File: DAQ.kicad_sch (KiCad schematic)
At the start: 32 parts, among them IC2 TEENSY_4.1, SW1 SW_Push_Open, SW2 SW_Push_Open, U3 CD-PA1616D

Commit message: added display
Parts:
- added U4: ~, symbol DAQcustom:NX4024T032
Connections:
- net +5V: now also U4.1 (Vdd)
- net GND: now also U4.2 (GND)
- net at IC2.28 (RX7): now also U4.4 (TX)
- net at IC2.29 (TX7): now also U4.3 (RX)
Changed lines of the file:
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@@
+    (stroke (width 0) (type default))
+  )
+  (wire (pts (xy 143.51 129.54) (xy 152.4 129.54))
     (stroke (width 0) (type default))
   )
@@
     (stroke (width 0) (type default))
   )
+  (wire (pts (xy 110.49 167.64) (xy 116.84 167.64))
+    (stroke (width 0) (type default))
+  )
   (wire (pts (xy 67.31 93.98) (xy 68.58 93.98))
     (stroke (width 0) (type default))
@@
     (stroke (width 0) (type default))
   )
+  (wire (pts (xy 146.05 132.08) (xy 152.4 132.08))
+    (stroke (width 0) (type default))
+  )
   (wire (pts (xy 69.85 148.59) (xy 80.01 148.59))
     (stroke (width 0) (type default))
@@
     (stroke (width 0) (type default))
   )
+  (wire (pts (xy 143.51 163.83) (xy 143.51 129.54))
+    (stroke (width 0) (type default))
+  )
   (polyline (pts (xy 227.33 64.77) (xy 238.76 64.77))
     (stroke (width 0) (type default))
@@
     (stroke (width 0) (type default))
   )
+  (wire (pts (xy 146.05 167.64) (xy 146.05 132.08))
+    (stroke (width 0) (type default))
+  )
   (polyline (pts (xy 118.11 129.54) (xy 118.11 152.4))
     (stroke (width 0) (type default))
@@
     (stroke (width 0) (type default))
   )
+  (wire (pts (xy 132.08 167.64) (xy 146.05 167.64))
+    (stroke (width 0) (type default))
+  )
   (wire (pts (xy 172.72 156.21) (xy 184.15 156.21))
     (stroke (width 0) (type default))
@@
     (stroke (width 0) (type default))
   )
+  (wire (pts (xy 132.08 163.83) (xy 143.51 163.83))
+    (stroke (width 0) (type default))
+  )
   (wire (pts (xy 109.22 78.74) (xy 125.73 78.74))
     (stroke (width 0) (type default))
@@
   )
   (wire (pts (xy 232.41 82.55) (xy 232.41 83.82))
+    (stroke (width 0) (type default))
+  )
+  (wire (pts (xy 110.49 163.83) (xy 116.84 163.83))
     (stroke (width 0) (type default))
   )
@@
     )
   )
+  (symbol (lib_id "power:+5V") (at 110.49 163.83 0) (unit 1)
+    (in_bom yes) (on_board yes) (dnp no) (fields_autoplaced)
+    (property "Reference" "#PWR022" (at 110.49 167.64 0)
+      (effects (font (size 1.27 1.27)) hide)
+    )
+    (property "Value" "+5V" (at 110.49 158.75 0)
+      (effects (font (size 1.27 1.27)))
+    )
+    (property "Footprint" "" (at 110.49 163.83 0)
+      (effects (font (size 1.27 1.27)) hide)
+    )
+    (property "Datasheet" "" (at 110.49 163.83 0)
+      (effects (font (size 1.27 1.27)) hide)
+    )
+    (pin "1")
+    (instances
+      (project "DAQ"
+        (path "/813e588e-265c-47f4-92de-e30a6c3791f8"
+          (reference "#PWR022") (unit 1)
+        )
+      )
+    )
+  )
   (symbol (lib_id "Device:R_Potentiometer") (at 33.02 139.7 0) (unit 1)
     (in_bom yes) (on_board yes) (dnp no) (fields_autoplaced)
@@
         (path "/813e588e-265c-47f4-92de-e30a6c3791f8"
           (reference "#PWR05") (unit 1)
+        )
+      )
+    )
+  )
+  (symbol (lib_id "DAQcustom:NX4024T032") (at 124.46 166.37 0) (unit 1)
+    (in_bom yes) (on_board yes) (dnp no) (fields_autoplaced)
+    (property "Reference" "U4" (at 124.46 157.48 0)
+      (effects (font (size 1.27 1.27)))
+    )
+    (property "Value" "~" (at 124.46 166.37 0)
+      (effects (font (size 1.27 1.27)))
+    )
+    (property "Footprint" "" (at 124.46 166.37 0)
+      (effects (font (size 1.27 1.27)) hide)
+    )
+    (property "Datasheet" "" (at 124.46 166.37 0)
+      (effects (font (size 1.27 1.27)) hide)
+    )
+    (pin "1")
+    (pin "2")
+    (pin "3")
+    (pin "4")
+    (instances
+      (project "DAQ"
+        (path "/813e588e-265c-47f4-92de-e30a6c3791f8"
+          (reference "U4") (unit 1)
         )
       )
@@
         )
       )
+    )
+  )
+  (symbol (lib_id "power:GND") (at 110.49 167.64 0) (unit 1)
+    (in_bom yes) (on_board yes) (dnp no) (fields_autoplaced)
+    (property "Reference" "#PWR023" (at 110.49 173.99 0)
+      (effects (font (size 1.27 1.27)) hide)
+    )
+    (property "Value" "GND" (at 110.49 172.72 0)
+      (effects (font (size 1.27 1.27)))
+    )
+    (property "Footprint" "" (at 110.49 167.64 0)
+      (effects (font (size 1.27 1.27)) hide)
+    )
+    (property "Datasheet" "" (at 110.49 167.64 0)
+      (effects (font (size 1.27 1.27)) hide)
+    )
+    (pin "1")
+    (instances
+      (project "DAQ"
+        (path "/813e588e-265c-47f4-92de-e30a6c3791f8"
+          (reference "#PWR023") (unit 1)
+        )
+      )

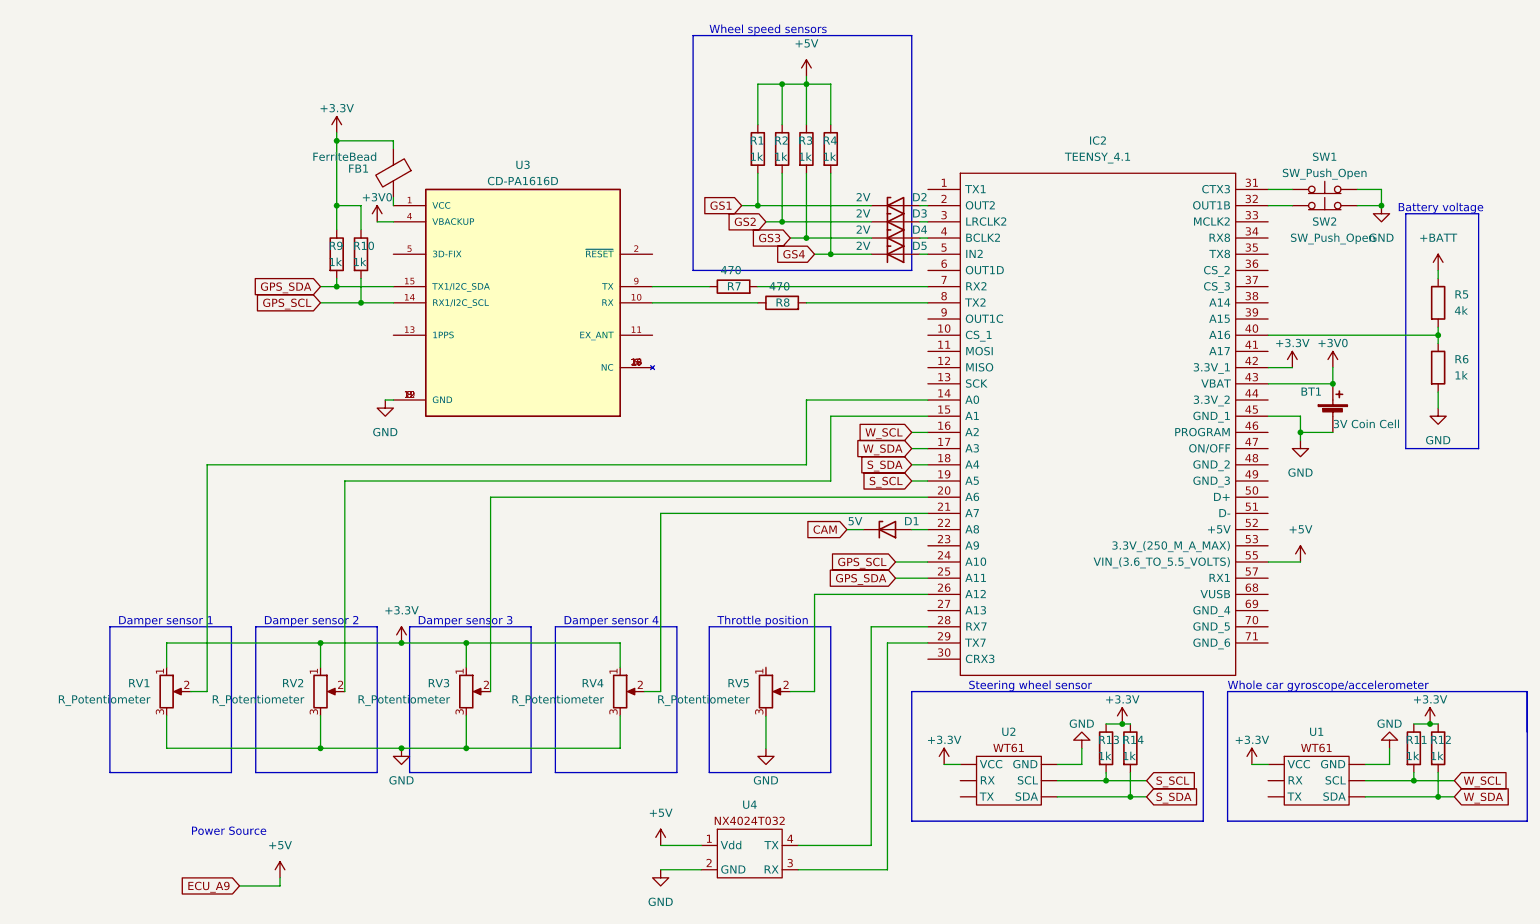
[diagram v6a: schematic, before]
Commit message: LCD added
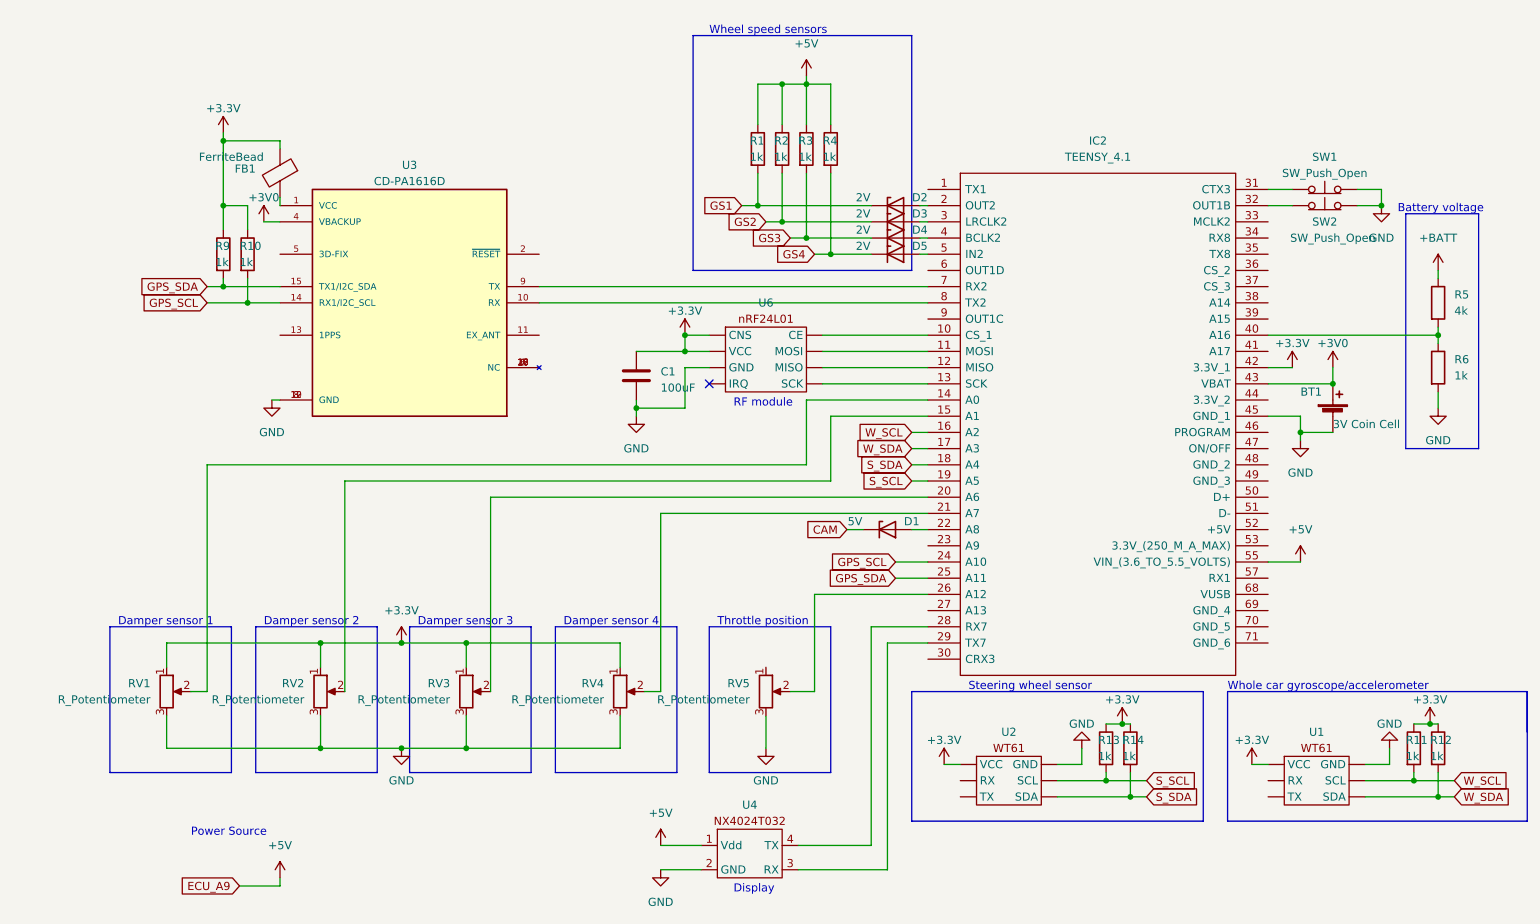
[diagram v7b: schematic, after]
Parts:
- removed R7, R8: 470, symbol Device:R
- added C1: 100uF, symbol Device:C
- added U6: ~, symbol DAQcustom:nRF24L01
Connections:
- net +3.3V: now also C1.1, U6. (VCC)
- net GND: now also C1.2, U6. (VCC)
- net at U3.10 (RX): now also IC2.8 (TX2)
- net at U3.9 (TX): now also IC2.7 (RX2)
- net at IC2.10 (CS_1): now also U6. (VCC)
- net at IC2.11 (MOSI): now also U6. (VCC)
- net at IC2.12 (MISO): now also U6. (VCC)
- net at IC2.13 (SCK): now also U6. (VCC)
- no-connect marks 0 -> 1
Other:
- note added: "Display"
- note added: "RF module"
- moved on the sheet: FB1, R10, R9, U3
